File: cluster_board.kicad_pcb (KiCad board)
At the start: 4 copper layers, 200 x 200 mm, 170 parts, among them J1 PICO_UART, J10 TILE_OUT_1, J11 TILE_OUT_2, J12 TILE_OUT_3, J13 TILE_OUT_4, J14 TILE_OUT_5, J15 TILE_OUT_6, J2 BOOT_I2C, J3 TILE_IN, U1 RP2354B, U10 RP2354B, U100 RP2354B, U101 RP2354B, U102 RP2354B, U103 RP2354B, U104 RP2354B, U105 RP2354B, U106 RP2354B, U107 RP2354B, U108 RP2354B, U109 RP2354B, U11 RP2354B, U110 RP2354B, U111 RP2354B, U112 RP2354B, U113 RP2354B, U114 RP2354B, U115 RP2354B, U116 RP2354B, U117 RP2354B, U118 RP2354B, U119 RP2354B, U12 RP2354B, U120 RP2354B, U121 TPS54560_A, U122 TPS54560_B, U13 RP2354B, U130 PCF8574, U131 PCF8574, U132 PCF8574, U133 PCF8574, U134 PCF8574, U135 PCF8574, U136 PCF8574, U137 PCF8574, U138 PCF8574A, U139 PCF8574A, U14 RP2354B, U140 PCF8574A, U141 PCF8574A, U142 PCF8574A, U143 PCF8574A, U144 PCF8574A, U145 74HC244, U146 74HC244, U147 74HC244, U148 74HC244, U149 74HC244, U15 RP2354B, U150 74HC244, U151 74HC244, U152 74HC244, U153 74HC244, U154 74HC244, U155 74HC244, U156 74HC244, U157 74HC244, U158 74HC244, U159 74HC244, U16 RP2354B, U17 RP2354B, U18 RP2354B, U19 RP2354B, U2 RP2354B, U20 RP2354B, U21 RP2354B, U22 RP2354B, U23 RP2354B, U24 RP2354B, U25 RP2354B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

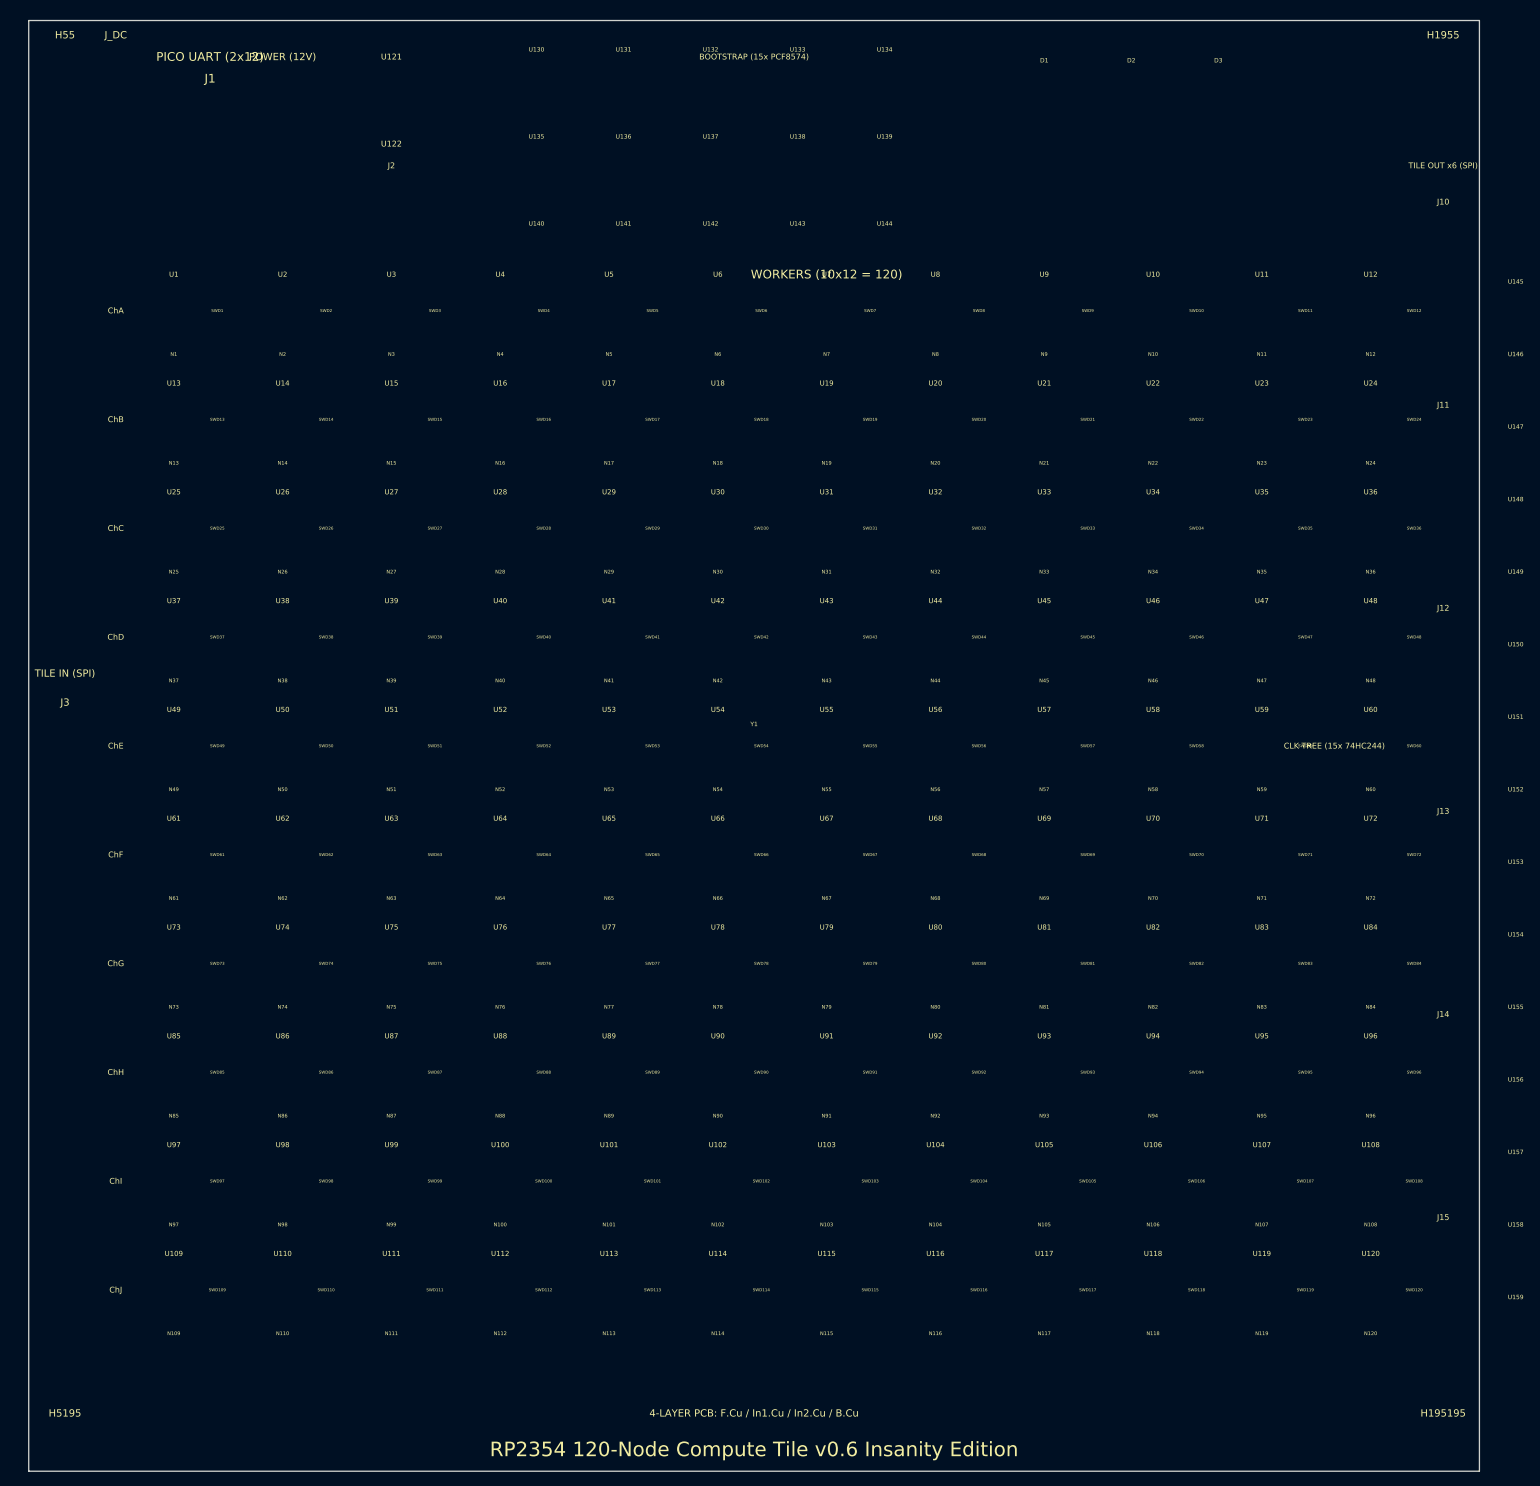
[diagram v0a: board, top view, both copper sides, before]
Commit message: Regenerate KiCad output files for v1.0 architecture
Co-authored-by: Copilot <223556219+Copilot@users.noreply.github.com>
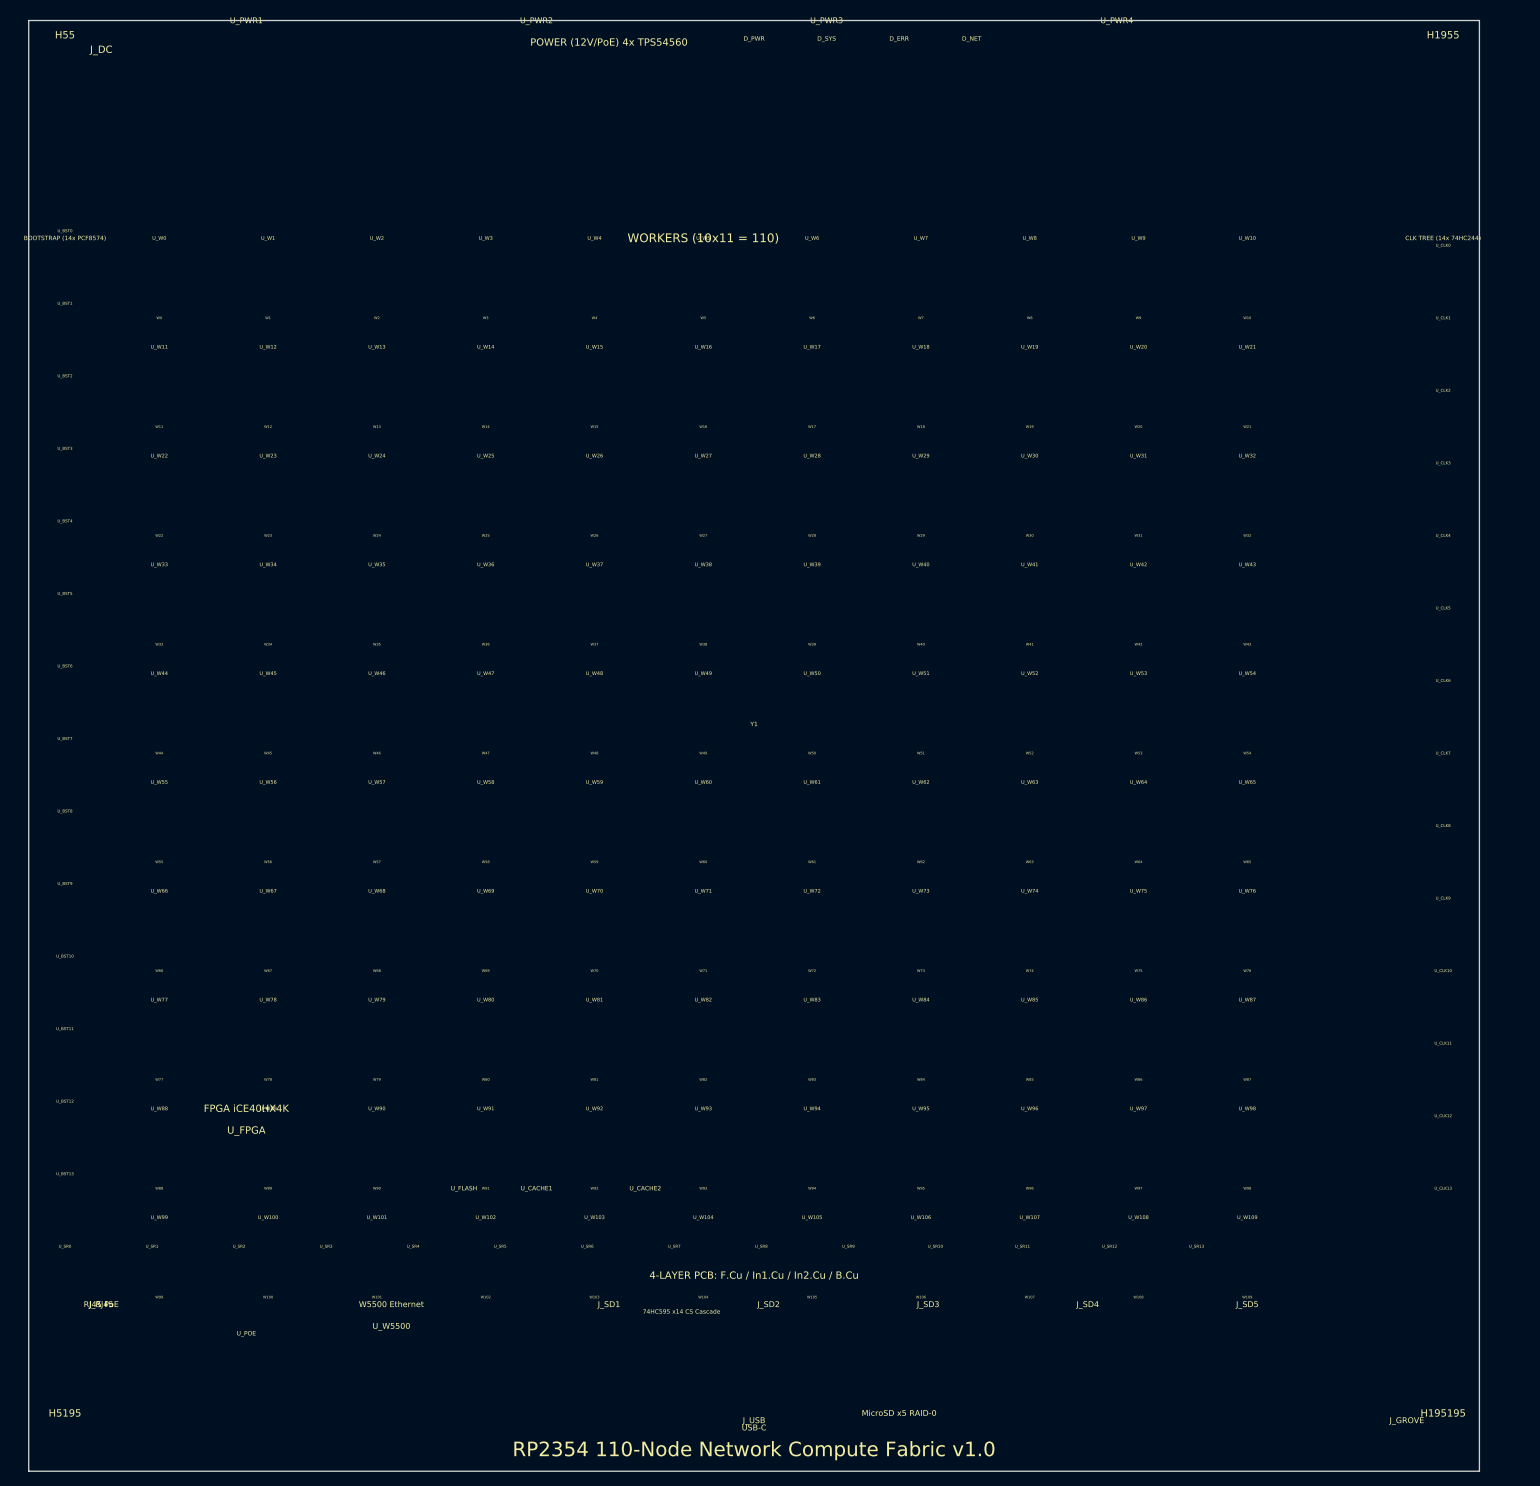
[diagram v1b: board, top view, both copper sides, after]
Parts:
- removed D1: PWR, LED_SMD:LED_0603_1608Metric
- removed D2: SYS, LED_SMD:LED_0603_1608Metric
- removed D3: ERR, LED_SMD:LED_0603_1608Metric
- removed J1: PICO_UART, Connector_PinHeader_2.54mm:PinHeader_2x12_P2.54mm_Vertical
- removed J10: TILE_OUT_1, Connector_JST:JST_PH_B4B-PH-K_1x04_P2.00mm_Vertical
- removed J11: TILE_OUT_2, Connector_JST:JST_PH_B4B-PH-K_1x04_P2.00mm_Vertical
- removed J12: TILE_OUT_3, Connector_JST:JST_PH_B4B-PH-K_1x04_P2.00mm_Vertical
- removed J13: TILE_OUT_4, Connector_JST:JST_PH_B4B-PH-K_1x04_P2.00mm_Vertical
- removed J14: TILE_OUT_5, Connector_JST:JST_PH_B4B-PH-K_1x04_P2.00mm_Vertical
- removed J15: TILE_OUT_6, Connector_JST:JST_PH_B4B-PH-K_1x04_P2.00mm_Vertical
- removed J2: BOOT_I2C, Connector_JST:JST_PH_B4B-PH-K_1x04_P2.00mm_Vertical
- removed J3: TILE_IN, Connector_JST:JST_PH_B4B-PH-K_1x04_P2.00mm_Vertical
- removed the J_DC at (12.0, 8.00)
- removed U1, U10, U100, U101, U102, U103, U104, U105, U106, U107, U108, U109, U11, U110, U111, U112, U113, U114, U115, U116, U117, U118, U119, U12, U120, U13, U14, U15, U16, U17, U18, U19, U2, U20, U21, U22, U23, U24, U25, U26, U27, U28, U29, U3, U30, U31, U32, U33, U34, U35, U36, U37, U38, U39, U4, U40, U41, U42, U43, U44, U45, U46, U47, U48, U49, U5, U50, U51, U52, U53, U54, U55, U56, U57, U58, U59, U6, U60, U61, U62, U63, U64, U65, U66, U67, U68, U69, U7, U70, U71, U72, U73, U74, U75, U76, U77, U78, U79, U8, U80, U81, U82, U83, U84, U85, U86, U87, U88, U89, U9, U90, U91, U92, U93, U94, U95, U96, U97, U98, U99: RP2354B, Package_DFN_QFN:QFN-80-1EP_10x10mm_P0.4mm_EP5.45x5.45mm
- removed U121: TPS54560_A, Package_SO:HSOP-8-1EP_3.9x4.9mm_P1.27mm_EP2.41x3.1mm
- removed U122: TPS54560_B, Package_SO:HSOP-8-1EP_3.9x4.9mm_P1.27mm_EP2.41x3.1mm
- removed U130, U131, U132, U133, U134, U135, U136, U137: PCF8574, Package_SO:SOIC-16_3.9x9.9mm_P1.27mm
- removed U138, U139, U140, U141, U142, U143, U144: PCF8574A, Package_SO:SOIC-16_3.9x9.9mm_P1.27mm
- removed U145, U146, U147, U148, U149, U150, U151, U152, U153, U154, U155, U156, U157, U158, U159: 74HC244, Package_SO:TSSOP-20_4.4x6.5mm_P0.65mm
- added D_ERR: ERR, LED_SMD:LED_0603_1608Metric, F.Cu at (120.0, 5.00)
- added D_NET: NET, LED_SMD:LED_0603_1608Metric, F.Cu at (130.0, 5.00)
- added D_PWR: PWR, LED_SMD:LED_0603_1608Metric, F.Cu at (100.0, 5.00)
- added D_SYS: SYS, LED_SMD:LED_0603_1608Metric, F.Cu at (110.0, 5.00)
- added J_DC: 12V_DC, TerminalBlock_Phoenix:TerminalBlock_Phoenix_PT-1,5-2-5.0-H_1x02_P5.00mm_Horizontal, F.Cu at (10.0, 10.0)
- added J_GROVE: Grove_I2C, Connector_JST:JST_PH_B4B-PH-K_1x04_P2.00mm_Vertical, F.Cu at (190.0, 198.0)
- added J_RJ45: RJ45_PoE, Connector_RJ:RJ45_Amphenol_ARJM11D7-805-AB-EW2, F.Cu at (10.0, 185.0)
- added J_SD1: MicroSD_1, Connector_Card:microSD_HC_Molex_104031-0811, F.Cu at (80.0, 185.0)
- added J_SD2: MicroSD_2, Connector_Card:microSD_HC_Molex_104031-0811, F.Cu at (102.0, 185.0)
- added J_SD3: MicroSD_3, Connector_Card:microSD_HC_Molex_104031-0811, F.Cu at (124.0, 185.0)
- added J_SD4: MicroSD_4, Connector_Card:microSD_HC_Molex_104031-0811, F.Cu at (146.0, 185.0)
- added J_SD5: MicroSD_5, Connector_Card:microSD_HC_Molex_104031-0811, F.Cu at (168.0, 185.0)
- added J_USB: USB_C, Connector_USB:USB_C_Receptacle_GCT_USB4105-xx-A_16P_TopMount_Horizontal, F.Cu at (100.0, 198.0)
- added U_BST0: PCF8574, Package_SO:SOIC-16_3.9x9.9mm_P1.27mm, F.Cu at (5.00, 35.0)
- added U_BST1: PCF8574, Package_SO:SOIC-16_3.9x9.9mm_P1.27mm, F.Cu at (5.00, 45.0)
- added U_BST10: PCF8574, Package_SO:SOIC-16_3.9x9.9mm_P1.27mm, F.Cu at (5.00, 135.0)
- added U_BST11: PCF8574, Package_SO:SOIC-16_3.9x9.9mm_P1.27mm, F.Cu at (5.00, 145.0)
- added U_BST12: PCF8574, Package_SO:SOIC-16_3.9x9.9mm_P1.27mm, F.Cu at (5.00, 155.0)
- added U_BST13: PCF8574, Package_SO:SOIC-16_3.9x9.9mm_P1.27mm, F.Cu at (5.00, 165.0)
- added U_BST2: PCF8574, Package_SO:SOIC-16_3.9x9.9mm_P1.27mm, F.Cu at (5.00, 55.0)
- added U_BST3: PCF8574, Package_SO:SOIC-16_3.9x9.9mm_P1.27mm, F.Cu at (5.00, 65.0)
- added U_BST4: PCF8574, Package_SO:SOIC-16_3.9x9.9mm_P1.27mm, F.Cu at (5.00, 75.0)
- added U_BST5: PCF8574, Package_SO:SOIC-16_3.9x9.9mm_P1.27mm, F.Cu at (5.00, 85.0)
- added U_BST6: PCF8574, Package_SO:SOIC-16_3.9x9.9mm_P1.27mm, F.Cu at (5.00, 95.0)
- added U_BST7: PCF8574, Package_SO:SOIC-16_3.9x9.9mm_P1.27mm, F.Cu at (5.00, 105.0)
- added U_BST8: PCF8574, Package_SO:SOIC-16_3.9x9.9mm_P1.27mm, F.Cu at (5.00, 115.0)
- added U_BST9: PCF8574, Package_SO:SOIC-16_3.9x9.9mm_P1.27mm, F.Cu at (5.00, 125.0)
- added U_CACHE1: APS6404L, Package_SO:SOP-8_3.9x4.9mm_P1.27mm, F.Cu at (70.0, 165.0)
- added U_CACHE2: APS6404L, Package_SO:SOP-8_3.9x4.9mm_P1.27mm, F.Cu at (85.0, 165.0)
- added U_CLK0: 74HC244, Package_SO:TSSOP-20_4.4x6.5mm_P0.65mm, F.Cu at (195.0, 35.0)
- added U_CLK1: 74HC244, Package_SO:TSSOP-20_4.4x6.5mm_P0.65mm, F.Cu at (195.0, 45.0)
- added U_CLK10: 74HC244, Package_SO:TSSOP-20_4.4x6.5mm_P0.65mm, F.Cu at (195.0, 135.0)
- added U_CLK11: 74HC244, Package_SO:TSSOP-20_4.4x6.5mm_P0.65mm, F.Cu at (195.0, 145.0)
- added U_CLK12: 74HC244, Package_SO:TSSOP-20_4.4x6.5mm_P0.65mm, F.Cu at (195.0, 155.0)
- added U_CLK13: 74HC244, Package_SO:TSSOP-20_4.4x6.5mm_P0.65mm, F.Cu at (195.0, 165.0)
- added U_CLK2: 74HC244, Package_SO:TSSOP-20_4.4x6.5mm_P0.65mm, F.Cu at (195.0, 55.0)
- added U_CLK3: 74HC244, Package_SO:TSSOP-20_4.4x6.5mm_P0.65mm, F.Cu at (195.0, 65.0)
- added U_CLK4: 74HC244, Package_SO:TSSOP-20_4.4x6.5mm_P0.65mm, F.Cu at (195.0, 75.0)
- added U_CLK5: 74HC244, Package_SO:TSSOP-20_4.4x6.5mm_P0.65mm, F.Cu at (195.0, 85.0)
- added U_CLK6: 74HC244, Package_SO:TSSOP-20_4.4x6.5mm_P0.65mm, F.Cu at (195.0, 95.0)
- added U_CLK7: 74HC244, Package_SO:TSSOP-20_4.4x6.5mm_P0.65mm, F.Cu at (195.0, 105.0)
- added U_CLK8: 74HC244, Package_SO:TSSOP-20_4.4x6.5mm_P0.65mm, F.Cu at (195.0, 115.0)
- added U_CLK9: 74HC244, Package_SO:TSSOP-20_4.4x6.5mm_P0.65mm, F.Cu at (195.0, 125.0)
- added U_FLASH: W25Q32, Package_SO:SOIC-8_3.9x4.9mm_P1.27mm, F.Cu at (60.0, 165.0)
- added U_FPGA: iCE40HX4K, Package_QFP:TQFP-144_20x20mm_P0.5mm, F.Cu at (30.0, 165.0)
- added U_POE: Ag9905, Package_SO:SOP-8_3.9x4.9mm_P1.27mm, F.Cu at (30.0, 185.0)
- added U_PSRAM0: LY68L6400, Package_SO:SOP-8_3.9x4.9mm_P1.27mm, B.Cu at (18.0, 35.0)
- added U_PSRAM1: LY68L6400, Package_SO:SOP-8_3.9x4.9mm_P1.27mm, B.Cu at (33.0, 35.0)
- added U_PSRAM10: LY68L6400, Package_SO:SOP-8_3.9x4.9mm_P1.27mm, B.Cu at (168.0, 35.0)
- added U_PSRAM100: LY68L6400, Package_SO:SOP-8_3.9x4.9mm_P1.27mm, B.Cu at (33.0, 170.0)
- added U_PSRAM101: LY68L6400, Package_SO:SOP-8_3.9x4.9mm_P1.27mm, B.Cu at (48.0, 170.0)
- added U_PSRAM102: LY68L6400, Package_SO:SOP-8_3.9x4.9mm_P1.27mm, B.Cu at (63.0, 170.0)
- added U_PSRAM103: LY68L6400, Package_SO:SOP-8_3.9x4.9mm_P1.27mm, B.Cu at (78.0, 170.0)
- added U_PSRAM104: LY68L6400, Package_SO:SOP-8_3.9x4.9mm_P1.27mm, B.Cu at (93.0, 170.0)
- added U_PSRAM105: LY68L6400, Package_SO:SOP-8_3.9x4.9mm_P1.27mm, B.Cu at (108.0, 170.0)
- added U_PSRAM106: LY68L6400, Package_SO:SOP-8_3.9x4.9mm_P1.27mm, B.Cu at (123.0, 170.0)
- added U_PSRAM107: LY68L6400, Package_SO:SOP-8_3.9x4.9mm_P1.27mm, B.Cu at (138.0, 170.0)
- added U_PSRAM108: LY68L6400, Package_SO:SOP-8_3.9x4.9mm_P1.27mm, B.Cu at (153.0, 170.0)
- added U_PSRAM109: LY68L6400, Package_SO:SOP-8_3.9x4.9mm_P1.27mm, B.Cu at (168.0, 170.0)
- added U_PSRAM11: LY68L6400, Package_SO:SOP-8_3.9x4.9mm_P1.27mm, B.Cu at (18.0, 50.0)
- added U_PSRAM12: LY68L6400, Package_SO:SOP-8_3.9x4.9mm_P1.27mm, B.Cu at (33.0, 50.0)
- added U_PSRAM13: LY68L6400, Package_SO:SOP-8_3.9x4.9mm_P1.27mm, B.Cu at (48.0, 50.0)
- added U_PSRAM14: LY68L6400, Package_SO:SOP-8_3.9x4.9mm_P1.27mm, B.Cu at (63.0, 50.0)
- added U_PSRAM15: LY68L6400, Package_SO:SOP-8_3.9x4.9mm_P1.27mm, B.Cu at (78.0, 50.0)
- added U_PSRAM16: LY68L6400, Package_SO:SOP-8_3.9x4.9mm_P1.27mm, B.Cu at (93.0, 50.0)
- added U_PSRAM17: LY68L6400, Package_SO:SOP-8_3.9x4.9mm_P1.27mm, B.Cu at (108.0, 50.0)
- added U_PSRAM18: LY68L6400, Package_SO:SOP-8_3.9x4.9mm_P1.27mm, B.Cu at (123.0, 50.0)
- added U_PSRAM19: LY68L6400, Package_SO:SOP-8_3.9x4.9mm_P1.27mm, B.Cu at (138.0, 50.0)
- added U_PSRAM2: LY68L6400, Package_SO:SOP-8_3.9x4.9mm_P1.27mm, B.Cu at (48.0, 35.0)
- added U_PSRAM20: LY68L6400, Package_SO:SOP-8_3.9x4.9mm_P1.27mm, B.Cu at (153.0, 50.0)
- added U_PSRAM21: LY68L6400, Package_SO:SOP-8_3.9x4.9mm_P1.27mm, B.Cu at (168.0, 50.0)
- added U_PSRAM22: LY68L6400, Package_SO:SOP-8_3.9x4.9mm_P1.27mm, B.Cu at (18.0, 65.0)
- added U_PSRAM23: LY68L6400, Package_SO:SOP-8_3.9x4.9mm_P1.27mm, B.Cu at (33.0, 65.0)
- added U_PSRAM24: LY68L6400, Package_SO:SOP-8_3.9x4.9mm_P1.27mm, B.Cu at (48.0, 65.0)
- added U_PSRAM25: LY68L6400, Package_SO:SOP-8_3.9x4.9mm_P1.27mm, B.Cu at (63.0, 65.0)
- added U_PSRAM26: LY68L6400, Package_SO:SOP-8_3.9x4.9mm_P1.27mm, B.Cu at (78.0, 65.0)
- added U_PSRAM27: LY68L6400, Package_SO:SOP-8_3.9x4.9mm_P1.27mm, B.Cu at (93.0, 65.0)
- added U_PSRAM28: LY68L6400, Package_SO:SOP-8_3.9x4.9mm_P1.27mm, B.Cu at (108.0, 65.0)
- added U_PSRAM29: LY68L6400, Package_SO:SOP-8_3.9x4.9mm_P1.27mm, B.Cu at (123.0, 65.0)
- added U_PSRAM3: LY68L6400, Package_SO:SOP-8_3.9x4.9mm_P1.27mm, B.Cu at (63.0, 35.0)
- added U_PSRAM30: LY68L6400, Package_SO:SOP-8_3.9x4.9mm_P1.27mm, B.Cu at (138.0, 65.0)
- added U_PSRAM31: LY68L6400, Package_SO:SOP-8_3.9x4.9mm_P1.27mm, B.Cu at (153.0, 65.0)
- added U_PSRAM32: LY68L6400, Package_SO:SOP-8_3.9x4.9mm_P1.27mm, B.Cu at (168.0, 65.0)
- added U_PSRAM33: LY68L6400, Package_SO:SOP-8_3.9x4.9mm_P1.27mm, B.Cu at (18.0, 80.0)
- added U_PSRAM34: LY68L6400, Package_SO:SOP-8_3.9x4.9mm_P1.27mm, B.Cu at (33.0, 80.0)
- added U_PSRAM35: LY68L6400, Package_SO:SOP-8_3.9x4.9mm_P1.27mm, B.Cu at (48.0, 80.0)
- added U_PSRAM36: LY68L6400, Package_SO:SOP-8_3.9x4.9mm_P1.27mm, B.Cu at (63.0, 80.0)
- added U_PSRAM37: LY68L6400, Package_SO:SOP-8_3.9x4.9mm_P1.27mm, B.Cu at (78.0, 80.0)
- added U_PSRAM38: LY68L6400, Package_SO:SOP-8_3.9x4.9mm_P1.27mm, B.Cu at (93.0, 80.0)
- added U_PSRAM39: LY68L6400, Package_SO:SOP-8_3.9x4.9mm_P1.27mm, B.Cu at (108.0, 80.0)
- added U_PSRAM4: LY68L6400, Package_SO:SOP-8_3.9x4.9mm_P1.27mm, B.Cu at (78.0, 35.0)
- added U_PSRAM40: LY68L6400, Package_SO:SOP-8_3.9x4.9mm_P1.27mm, B.Cu at (123.0, 80.0)
- added U_PSRAM41: LY68L6400, Package_SO:SOP-8_3.9x4.9mm_P1.27mm, B.Cu at (138.0, 80.0)
- added U_PSRAM42: LY68L6400, Package_SO:SOP-8_3.9x4.9mm_P1.27mm, B.Cu at (153.0, 80.0)
- added U_PSRAM43: LY68L6400, Package_SO:SOP-8_3.9x4.9mm_P1.27mm, B.Cu at (168.0, 80.0)
- added U_PSRAM44: LY68L6400, Package_SO:SOP-8_3.9x4.9mm_P1.27mm, B.Cu at (18.0, 95.0)
- added U_PSRAM45: LY68L6400, Package_SO:SOP-8_3.9x4.9mm_P1.27mm, B.Cu at (33.0, 95.0)
- added U_PSRAM46: LY68L6400, Package_SO:SOP-8_3.9x4.9mm_P1.27mm, B.Cu at (48.0, 95.0)
- added U_PSRAM47: LY68L6400, Package_SO:SOP-8_3.9x4.9mm_P1.27mm, B.Cu at (63.0, 95.0)
- added U_PSRAM48: LY68L6400, Package_SO:SOP-8_3.9x4.9mm_P1.27mm, B.Cu at (78.0, 95.0)
- added U_PSRAM49: LY68L6400, Package_SO:SOP-8_3.9x4.9mm_P1.27mm, B.Cu at (93.0, 95.0)
- added U_PSRAM5: LY68L6400, Package_SO:SOP-8_3.9x4.9mm_P1.27mm, B.Cu at (93.0, 35.0)
- added U_PSRAM50: LY68L6400, Package_SO:SOP-8_3.9x4.9mm_P1.27mm, B.Cu at (108.0, 95.0)
- added U_PSRAM51: LY68L6400, Package_SO:SOP-8_3.9x4.9mm_P1.27mm, B.Cu at (123.0, 95.0)
- added U_PSRAM52: LY68L6400, Package_SO:SOP-8_3.9x4.9mm_P1.27mm, B.Cu at (138.0, 95.0)
- added U_PSRAM53: LY68L6400, Package_SO:SOP-8_3.9x4.9mm_P1.27mm, B.Cu at (153.0, 95.0)
- added U_PSRAM54: LY68L6400, Package_SO:SOP-8_3.9x4.9mm_P1.27mm, B.Cu at (168.0, 95.0)
- added U_PSRAM55: LY68L6400, Package_SO:SOP-8_3.9x4.9mm_P1.27mm, B.Cu at (18.0, 110.0)
- added U_PSRAM56: LY68L6400, Package_SO:SOP-8_3.9x4.9mm_P1.27mm, B.Cu at (33.0, 110.0)
- added U_PSRAM57: LY68L6400, Package_SO:SOP-8_3.9x4.9mm_P1.27mm, B.Cu at (48.0, 110.0)
- added U_PSRAM58: LY68L6400, Package_SO:SOP-8_3.9x4.9mm_P1.27mm, B.Cu at (63.0, 110.0)
- added U_PSRAM59: LY68L6400, Package_SO:SOP-8_3.9x4.9mm_P1.27mm, B.Cu at (78.0, 110.0)
- added U_PSRAM6: LY68L6400, Package_SO:SOP-8_3.9x4.9mm_P1.27mm, B.Cu at (108.0, 35.0)
- added U_PSRAM60: LY68L6400, Package_SO:SOP-8_3.9x4.9mm_P1.27mm, B.Cu at (93.0, 110.0)
- added U_PSRAM61: LY68L6400, Package_SO:SOP-8_3.9x4.9mm_P1.27mm, B.Cu at (108.0, 110.0)
- added U_PSRAM62: LY68L6400, Package_SO:SOP-8_3.9x4.9mm_P1.27mm, B.Cu at (123.0, 110.0)
- added U_PSRAM63: LY68L6400, Package_SO:SOP-8_3.9x4.9mm_P1.27mm, B.Cu at (138.0, 110.0)
- added U_PSRAM64: LY68L6400, Package_SO:SOP-8_3.9x4.9mm_P1.27mm, B.Cu at (153.0, 110.0)
- added U_PSRAM65: LY68L6400, Package_SO:SOP-8_3.9x4.9mm_P1.27mm, B.Cu at (168.0, 110.0)
- added U_PSRAM66: LY68L6400, Package_SO:SOP-8_3.9x4.9mm_P1.27mm, B.Cu at (18.0, 125.0)
- added U_PSRAM67: LY68L6400, Package_SO:SOP-8_3.9x4.9mm_P1.27mm, B.Cu at (33.0, 125.0)
- added U_PSRAM68: LY68L6400, Package_SO:SOP-8_3.9x4.9mm_P1.27mm, B.Cu at (48.0, 125.0)
- added U_PSRAM69: LY68L6400, Package_SO:SOP-8_3.9x4.9mm_P1.27mm, B.Cu at (63.0, 125.0)
- added U_PSRAM7: LY68L6400, Package_SO:SOP-8_3.9x4.9mm_P1.27mm, B.Cu at (123.0, 35.0)
- added U_PSRAM70: LY68L6400, Package_SO:SOP-8_3.9x4.9mm_P1.27mm, B.Cu at (78.0, 125.0)
- added U_PSRAM71: LY68L6400, Package_SO:SOP-8_3.9x4.9mm_P1.27mm, B.Cu at (93.0, 125.0)
- added U_PSRAM72: LY68L6400, Package_SO:SOP-8_3.9x4.9mm_P1.27mm, B.Cu at (108.0, 125.0)
- added U_PSRAM73: LY68L6400, Package_SO:SOP-8_3.9x4.9mm_P1.27mm, B.Cu at (123.0, 125.0)
- added U_PSRAM74: LY68L6400, Package_SO:SOP-8_3.9x4.9mm_P1.27mm, B.Cu at (138.0, 125.0)
- added U_PSRAM75: LY68L6400, Package_SO:SOP-8_3.9x4.9mm_P1.27mm, B.Cu at (153.0, 125.0)
- added U_PSRAM76: LY68L6400, Package_SO:SOP-8_3.9x4.9mm_P1.27mm, B.Cu at (168.0, 125.0)
- added U_PSRAM77: LY68L6400, Package_SO:SOP-8_3.9x4.9mm_P1.27mm, B.Cu at (18.0, 140.0)
- added U_PSRAM78: LY68L6400, Package_SO:SOP-8_3.9x4.9mm_P1.27mm, B.Cu at (33.0, 140.0)
- added U_PSRAM79: LY68L6400, Package_SO:SOP-8_3.9x4.9mm_P1.27mm, B.Cu at (48.0, 140.0)
- added U_PSRAM8: LY68L6400, Package_SO:SOP-8_3.9x4.9mm_P1.27mm, B.Cu at (138.0, 35.0)
- added U_PSRAM80: LY68L6400, Package_SO:SOP-8_3.9x4.9mm_P1.27mm, B.Cu at (63.0, 140.0)
- added U_PSRAM81: LY68L6400, Package_SO:SOP-8_3.9x4.9mm_P1.27mm, B.Cu at (78.0, 140.0)
- added U_PSRAM82: LY68L6400, Package_SO:SOP-8_3.9x4.9mm_P1.27mm, B.Cu at (93.0, 140.0)
- added U_PSRAM83: LY68L6400, Package_SO:SOP-8_3.9x4.9mm_P1.27mm, B.Cu at (108.0, 140.0)
- added U_PSRAM84: LY68L6400, Package_SO:SOP-8_3.9x4.9mm_P1.27mm, B.Cu at (123.0, 140.0)
- added U_PSRAM85: LY68L6400, Package_SO:SOP-8_3.9x4.9mm_P1.27mm, B.Cu at (138.0, 140.0)
- added U_PSRAM86: LY68L6400, Package_SO:SOP-8_3.9x4.9mm_P1.27mm, B.Cu at (153.0, 140.0)
- added U_PSRAM87: LY68L6400, Package_SO:SOP-8_3.9x4.9mm_P1.27mm, B.Cu at (168.0, 140.0)
- added U_PSRAM88: LY68L6400, Package_SO:SOP-8_3.9x4.9mm_P1.27mm, B.Cu at (18.0, 155.0)
- added U_PSRAM89: LY68L6400, Package_SO:SOP-8_3.9x4.9mm_P1.27mm, B.Cu at (33.0, 155.0)
- added U_PSRAM9: LY68L6400, Package_SO:SOP-8_3.9x4.9mm_P1.27mm, B.Cu at (153.0, 35.0)
- added U_PSRAM90: LY68L6400, Package_SO:SOP-8_3.9x4.9mm_P1.27mm, B.Cu at (48.0, 155.0)
- added U_PSRAM91: LY68L6400, Package_SO:SOP-8_3.9x4.9mm_P1.27mm, B.Cu at (63.0, 155.0)
- added U_PSRAM92: LY68L6400, Package_SO:SOP-8_3.9x4.9mm_P1.27mm, B.Cu at (78.0, 155.0)
- added U_PSRAM93: LY68L6400, Package_SO:SOP-8_3.9x4.9mm_P1.27mm, B.Cu at (93.0, 155.0)
- added U_PSRAM94: LY68L6400, Package_SO:SOP-8_3.9x4.9mm_P1.27mm, B.Cu at (108.0, 155.0)
- added U_PSRAM95: LY68L6400, Package_SO:SOP-8_3.9x4.9mm_P1.27mm, B.Cu at (123.0, 155.0)
- added U_PSRAM96: LY68L6400, Package_SO:SOP-8_3.9x4.9mm_P1.27mm, B.Cu at (138.0, 155.0)
- added U_PSRAM97: LY68L6400, Package_SO:SOP-8_3.9x4.9mm_P1.27mm, B.Cu at (153.0, 155.0)
- added U_PSRAM98: LY68L6400, Package_SO:SOP-8_3.9x4.9mm_P1.27mm, B.Cu at (168.0, 155.0)
- added U_PSRAM99: LY68L6400, Package_SO:SOP-8_3.9x4.9mm_P1.27mm, B.Cu at (18.0, 170.0)
- added U_PWR1: TPS54560_Z1, Package_SO:HSOP-8-1EP_3.9x4.9mm_P1.27mm_EP2.41x3.1mm, F.Cu at (30.0, 5.00)
- added U_PWR2: TPS54560_Z2, Package_SO:HSOP-8-1EP_3.9x4.9mm_P1.27mm_EP2.41x3.1mm, F.Cu at (70.0, 5.00)
- added U_PWR3: TPS54560_Z3, Package_SO:HSOP-8-1EP_3.9x4.9mm_P1.27mm_EP2.41x3.1mm, F.Cu at (110.0, 5.00)
- added U_PWR4: TPS54560_Z4, Package_SO:HSOP-8-1EP_3.9x4.9mm_P1.27mm_EP2.41x3.1mm, F.Cu at (150.0, 5.00)
- added U_SR0: 74HC595, Package_SO:SOIC-16_3.9x9.9mm_P1.27mm, F.Cu at (5.00, 175.0)
- added U_SR1: 74HC595, Package_SO:SOIC-16_3.9x9.9mm_P1.27mm, F.Cu at (17.0, 175.0)
- added U_SR10: 74HC595, Package_SO:SOIC-16_3.9x9.9mm_P1.27mm, F.Cu at (125.0, 175.0)
- added U_SR11: 74HC595, Package_SO:SOIC-16_3.9x9.9mm_P1.27mm, F.Cu at (137.0, 175.0)
- added U_SR12: 74HC595, Package_SO:SOIC-16_3.9x9.9mm_P1.27mm, F.Cu at (149.0, 175.0)
- added U_SR13: 74HC595, Package_SO:SOIC-16_3.9x9.9mm_P1.27mm, F.Cu at (161.0, 175.0)
- added U_SR2: 74HC595, Package_SO:SOIC-16_3.9x9.9mm_P1.27mm, F.Cu at (29.0, 175.0)
- added U_SR3: 74HC595, Package_SO:SOIC-16_3.9x9.9mm_P1.27mm, F.Cu at (41.0, 175.0)
- added U_SR4: 74HC595, Package_SO:SOIC-16_3.9x9.9mm_P1.27mm, F.Cu at (53.0, 175.0)
- added U_SR5: 74HC595, Package_SO:SOIC-16_3.9x9.9mm_P1.27mm, F.Cu at (65.0, 175.0)
- added U_SR6: 74HC595, Package_SO:SOIC-16_3.9x9.9mm_P1.27mm, F.Cu at (77.0, 175.0)
- added U_SR7: 74HC595, Package_SO:SOIC-16_3.9x9.9mm_P1.27mm, F.Cu at (89.0, 175.0)
- added U_SR8: 74HC595, Package_SO:SOIC-16_3.9x9.9mm_P1.27mm, F.Cu at (101.0, 175.0)
- added U_SR9: 74HC595, Package_SO:SOIC-16_3.9x9.9mm_P1.27mm, F.Cu at (113.0, 175.0)
- added U_W0: RP2354B, Package_DFN_QFN:QFN-80-1EP_10x10mm_P0.4mm_EP5.45x5.45mm, F.Cu at (18.0, 35.0)
- added U_W1: RP2354B, Package_DFN_QFN:QFN-80-1EP_10x10mm_P0.4mm_EP5.45x5.45mm, F.Cu at (33.0, 35.0)
- added U_W10: RP2354B, Package_DFN_QFN:QFN-80-1EP_10x10mm_P0.4mm_EP5.45x5.45mm, F.Cu at (168.0, 35.0)
- added U_W100: RP2354B, Package_DFN_QFN:QFN-80-1EP_10x10mm_P0.4mm_EP5.45x5.45mm, F.Cu at (33.0, 170.0)
- added U_W101: RP2354B, Package_DFN_QFN:QFN-80-1EP_10x10mm_P0.4mm_EP5.45x5.45mm, F.Cu at (48.0, 170.0)
- added U_W102: RP2354B, Package_DFN_QFN:QFN-80-1EP_10x10mm_P0.4mm_EP5.45x5.45mm, F.Cu at (63.0, 170.0)
- added U_W103: RP2354B, Package_DFN_QFN:QFN-80-1EP_10x10mm_P0.4mm_EP5.45x5.45mm, F.Cu at (78.0, 170.0)
- added U_W104: RP2354B, Package_DFN_QFN:QFN-80-1EP_10x10mm_P0.4mm_EP5.45x5.45mm, F.Cu at (93.0, 170.0)
- added U_W105: RP2354B, Package_DFN_QFN:QFN-80-1EP_10x10mm_P0.4mm_EP5.45x5.45mm, F.Cu at (108.0, 170.0)
- added U_W106: RP2354B, Package_DFN_QFN:QFN-80-1EP_10x10mm_P0.4mm_EP5.45x5.45mm, F.Cu at (123.0, 170.0)
- added U_W107: RP2354B, Package_DFN_QFN:QFN-80-1EP_10x10mm_P0.4mm_EP5.45x5.45mm, F.Cu at (138.0, 170.0)
- added U_W108: RP2354B, Package_DFN_QFN:QFN-80-1EP_10x10mm_P0.4mm_EP5.45x5.45mm, F.Cu at (153.0, 170.0)
- added U_W109: RP2354B, Package_DFN_QFN:QFN-80-1EP_10x10mm_P0.4mm_EP5.45x5.45mm, F.Cu at (168.0, 170.0)
- added U_W11: RP2354B, Package_DFN_QFN:QFN-80-1EP_10x10mm_P0.4mm_EP5.45x5.45mm, F.Cu at (18.0, 50.0)
- added U_W12: RP2354B, Package_DFN_QFN:QFN-80-1EP_10x10mm_P0.4mm_EP5.45x5.45mm, F.Cu at (33.0, 50.0)
- added U_W13: RP2354B, Package_DFN_QFN:QFN-80-1EP_10x10mm_P0.4mm_EP5.45x5.45mm, F.Cu at (48.0, 50.0)
- added U_W14: RP2354B, Package_DFN_QFN:QFN-80-1EP_10x10mm_P0.4mm_EP5.45x5.45mm, F.Cu at (63.0, 50.0)
- added U_W15: RP2354B, Package_DFN_QFN:QFN-80-1EP_10x10mm_P0.4mm_EP5.45x5.45mm, F.Cu at (78.0, 50.0)
- added U_W16: RP2354B, Package_DFN_QFN:QFN-80-1EP_10x10mm_P0.4mm_EP5.45x5.45mm, F.Cu at (93.0, 50.0)
- added U_W17: RP2354B, Package_DFN_QFN:QFN-80-1EP_10x10mm_P0.4mm_EP5.45x5.45mm, F.Cu at (108.0, 50.0)
- added U_W18: RP2354B, Package_DFN_QFN:QFN-80-1EP_10x10mm_P0.4mm_EP5.45x5.45mm, F.Cu at (123.0, 50.0)
- added U_W19: RP2354B, Package_DFN_QFN:QFN-80-1EP_10x10mm_P0.4mm_EP5.45x5.45mm, F.Cu at (138.0, 50.0)
- added U_W2: RP2354B, Package_DFN_QFN:QFN-80-1EP_10x10mm_P0.4mm_EP5.45x5.45mm, F.Cu at (48.0, 35.0)
- added U_W20: RP2354B, Package_DFN_QFN:QFN-80-1EP_10x10mm_P0.4mm_EP5.45x5.45mm, F.Cu at (153.0, 50.0)
- added U_W21: RP2354B, Package_DFN_QFN:QFN-80-1EP_10x10mm_P0.4mm_EP5.45x5.45mm, F.Cu at (168.0, 50.0)
- added U_W22: RP2354B, Package_DFN_QFN:QFN-80-1EP_10x10mm_P0.4mm_EP5.45x5.45mm, F.Cu at (18.0, 65.0)
- added U_W23: RP2354B, Package_DFN_QFN:QFN-80-1EP_10x10mm_P0.4mm_EP5.45x5.45mm, F.Cu at (33.0, 65.0)
- added U_W24: RP2354B, Package_DFN_QFN:QFN-80-1EP_10x10mm_P0.4mm_EP5.45x5.45mm, F.Cu at (48.0, 65.0)
- added U_W25: RP2354B, Package_DFN_QFN:QFN-80-1EP_10x10mm_P0.4mm_EP5.45x5.45mm, F.Cu at (63.0, 65.0)
- added U_W26: RP2354B, Package_DFN_QFN:QFN-80-1EP_10x10mm_P0.4mm_EP5.45x5.45mm, F.Cu at (78.0, 65.0)
- added U_W27: RP2354B, Package_DFN_QFN:QFN-80-1EP_10x10mm_P0.4mm_EP5.45x5.45mm, F.Cu at (93.0, 65.0)
- added U_W28: RP2354B, Package_DFN_QFN:QFN-80-1EP_10x10mm_P0.4mm_EP5.45x5.45mm, F.Cu at (108.0, 65.0)
- added U_W29: RP2354B, Package_DFN_QFN:QFN-80-1EP_10x10mm_P0.4mm_EP5.45x5.45mm, F.Cu at (123.0, 65.0)
- added U_W3: RP2354B, Package_DFN_QFN:QFN-80-1EP_10x10mm_P0.4mm_EP5.45x5.45mm, F.Cu at (63.0, 35.0)
- added U_W30: RP2354B, Package_DFN_QFN:QFN-80-1EP_10x10mm_P0.4mm_EP5.45x5.45mm, F.Cu at (138.0, 65.0)
- added U_W31: RP2354B, Package_DFN_QFN:QFN-80-1EP_10x10mm_P0.4mm_EP5.45x5.45mm, F.Cu at (153.0, 65.0)
- added U_W32: RP2354B, Package_DFN_QFN:QFN-80-1EP_10x10mm_P0.4mm_EP5.45x5.45mm, F.Cu at (168.0, 65.0)
- added U_W33: RP2354B, Package_DFN_QFN:QFN-80-1EP_10x10mm_P0.4mm_EP5.45x5.45mm, F.Cu at (18.0, 80.0)
- added U_W34: RP2354B, Package_DFN_QFN:QFN-80-1EP_10x10mm_P0.4mm_EP5.45x5.45mm, F.Cu at (33.0, 80.0)
- added U_W35: RP2354B, Package_DFN_QFN:QFN-80-1EP_10x10mm_P0.4mm_EP5.45x5.45mm, F.Cu at (48.0, 80.0)
- added U_W36: RP2354B, Package_DFN_QFN:QFN-80-1EP_10x10mm_P0.4mm_EP5.45x5.45mm, F.Cu at (63.0, 80.0)
- added U_W37: RP2354B, Package_DFN_QFN:QFN-80-1EP_10x10mm_P0.4mm_EP5.45x5.45mm, F.Cu at (78.0, 80.0)
- added U_W38: RP2354B, Package_DFN_QFN:QFN-80-1EP_10x10mm_P0.4mm_EP5.45x5.45mm, F.Cu at (93.0, 80.0)
- added U_W39: RP2354B, Package_DFN_QFN:QFN-80-1EP_10x10mm_P0.4mm_EP5.45x5.45mm, F.Cu at (108.0, 80.0)
- added U_W4: RP2354B, Package_DFN_QFN:QFN-80-1EP_10x10mm_P0.4mm_EP5.45x5.45mm, F.Cu at (78.0, 35.0)
- added U_W40: RP2354B, Package_DFN_QFN:QFN-80-1EP_10x10mm_P0.4mm_EP5.45x5.45mm, F.Cu at (123.0, 80.0)
- added U_W41: RP2354B, Package_DFN_QFN:QFN-80-1EP_10x10mm_P0.4mm_EP5.45x5.45mm, F.Cu at (138.0, 80.0)
- added U_W42: RP2354B, Package_DFN_QFN:QFN-80-1EP_10x10mm_P0.4mm_EP5.45x5.45mm, F.Cu at (153.0, 80.0)
- added U_W43: RP2354B, Package_DFN_QFN:QFN-80-1EP_10x10mm_P0.4mm_EP5.45x5.45mm, F.Cu at (168.0, 80.0)
- added U_W44: RP2354B, Package_DFN_QFN:QFN-80-1EP_10x10mm_P0.4mm_EP5.45x5.45mm, F.Cu at (18.0, 95.0)
- added U_W45: RP2354B, Package_DFN_QFN:QFN-80-1EP_10x10mm_P0.4mm_EP5.45x5.45mm, F.Cu at (33.0, 95.0)
- added U_W46: RP2354B, Package_DFN_QFN:QFN-80-1EP_10x10mm_P0.4mm_EP5.45x5.45mm, F.Cu at (48.0, 95.0)
- added U_W47: RP2354B, Package_DFN_QFN:QFN-80-1EP_10x10mm_P0.4mm_EP5.45x5.45mm, F.Cu at (63.0, 95.0)
- added U_W48: RP2354B, Package_DFN_QFN:QFN-80-1EP_10x10mm_P0.4mm_EP5.45x5.45mm, F.Cu at (78.0, 95.0)
- added U_W49: RP2354B, Package_DFN_QFN:QFN-80-1EP_10x10mm_P0.4mm_EP5.45x5.45mm, F.Cu at (93.0, 95.0)
- added U_W5: RP2354B, Package_DFN_QFN:QFN-80-1EP_10x10mm_P0.4mm_EP5.45x5.45mm, F.Cu at (93.0, 35.0)
- added U_W50: RP2354B, Package_DFN_QFN:QFN-80-1EP_10x10mm_P0.4mm_EP5.45x5.45mm, F.Cu at (108.0, 95.0)
- added U_W51: RP2354B, Package_DFN_QFN:QFN-80-1EP_10x10mm_P0.4mm_EP5.45x5.45mm, F.Cu at (123.0, 95.0)
- added U_W52: RP2354B, Package_DFN_QFN:QFN-80-1EP_10x10mm_P0.4mm_EP5.45x5.45mm, F.Cu at (138.0, 95.0)
- added U_W53: RP2354B, Package_DFN_QFN:QFN-80-1EP_10x10mm_P0.4mm_EP5.45x5.45mm, F.Cu at (153.0, 95.0)
- added U_W54: RP2354B, Package_DFN_QFN:QFN-80-1EP_10x10mm_P0.4mm_EP5.45x5.45mm, F.Cu at (168.0, 95.0)
- added U_W55: RP2354B, Package_DFN_QFN:QFN-80-1EP_10x10mm_P0.4mm_EP5.45x5.45mm, F.Cu at (18.0, 110.0)
- added U_W5500: W5500, Package_DFN_QFN:QFN-48-1EP_7x7mm_P0.5mm_EP5.15x5.15mm, F.Cu at (50.0, 185.0)
- added U_W56: RP2354B, Package_DFN_QFN:QFN-80-1EP_10x10mm_P0.4mm_EP5.45x5.45mm, F.Cu at (33.0, 110.0)
- added U_W57: RP2354B, Package_DFN_QFN:QFN-80-1EP_10x10mm_P0.4mm_EP5.45x5.45mm, F.Cu at (48.0, 110.0)
- added U_W58: RP2354B, Package_DFN_QFN:QFN-80-1EP_10x10mm_P0.4mm_EP5.45x5.45mm, F.Cu at (63.0, 110.0)
- added U_W59: RP2354B, Package_DFN_QFN:QFN-80-1EP_10x10mm_P0.4mm_EP5.45x5.45mm, F.Cu at (78.0, 110.0)
- added U_W6: RP2354B, Package_DFN_QFN:QFN-80-1EP_10x10mm_P0.4mm_EP5.45x5.45mm, F.Cu at (108.0, 35.0)
- added U_W60: RP2354B, Package_DFN_QFN:QFN-80-1EP_10x10mm_P0.4mm_EP5.45x5.45mm, F.Cu at (93.0, 110.0)
- added U_W61: RP2354B, Package_DFN_QFN:QFN-80-1EP_10x10mm_P0.4mm_EP5.45x5.45mm, F.Cu at (108.0, 110.0)
- added U_W62: RP2354B, Package_DFN_QFN:QFN-80-1EP_10x10mm_P0.4mm_EP5.45x5.45mm, F.Cu at (123.0, 110.0)
- added U_W63: RP2354B, Package_DFN_QFN:QFN-80-1EP_10x10mm_P0.4mm_EP5.45x5.45mm, F.Cu at (138.0, 110.0)
- added U_W64: RP2354B, Package_DFN_QFN:QFN-80-1EP_10x10mm_P0.4mm_EP5.45x5.45mm, F.Cu at (153.0, 110.0)
- added U_W65: RP2354B, Package_DFN_QFN:QFN-80-1EP_10x10mm_P0.4mm_EP5.45x5.45mm, F.Cu at (168.0, 110.0)
- added U_W66: RP2354B, Package_DFN_QFN:QFN-80-1EP_10x10mm_P0.4mm_EP5.45x5.45mm, F.Cu at (18.0, 125.0)
- added U_W67: RP2354B, Package_DFN_QFN:QFN-80-1EP_10x10mm_P0.4mm_EP5.45x5.45mm, F.Cu at (33.0, 125.0)
- added U_W68: RP2354B, Package_DFN_QFN:QFN-80-1EP_10x10mm_P0.4mm_EP5.45x5.45mm, F.Cu at (48.0, 125.0)
- added U_W69: RP2354B, Package_DFN_QFN:QFN-80-1EP_10x10mm_P0.4mm_EP5.45x5.45mm, F.Cu at (63.0, 125.0)
- added U_W7: RP2354B, Package_DFN_QFN:QFN-80-1EP_10x10mm_P0.4mm_EP5.45x5.45mm, F.Cu at (123.0, 35.0)
- added U_W70: RP2354B, Package_DFN_QFN:QFN-80-1EP_10x10mm_P0.4mm_EP5.45x5.45mm, F.Cu at (78.0, 125.0)
- added U_W71: RP2354B, Package_DFN_QFN:QFN-80-1EP_10x10mm_P0.4mm_EP5.45x5.45mm, F.Cu at (93.0, 125.0)
- added U_W72: RP2354B, Package_DFN_QFN:QFN-80-1EP_10x10mm_P0.4mm_EP5.45x5.45mm, F.Cu at (108.0, 125.0)
- added U_W73: RP2354B, Package_DFN_QFN:QFN-80-1EP_10x10mm_P0.4mm_EP5.45x5.45mm, F.Cu at (123.0, 125.0)
- added U_W74: RP2354B, Package_DFN_QFN:QFN-80-1EP_10x10mm_P0.4mm_EP5.45x5.45mm, F.Cu at (138.0, 125.0)
- added U_W75: RP2354B, Package_DFN_QFN:QFN-80-1EP_10x10mm_P0.4mm_EP5.45x5.45mm, F.Cu at (153.0, 125.0)
- added U_W76: RP2354B, Package_DFN_QFN:QFN-80-1EP_10x10mm_P0.4mm_EP5.45x5.45mm, F.Cu at (168.0, 125.0)
- added U_W77: RP2354B, Package_DFN_QFN:QFN-80-1EP_10x10mm_P0.4mm_EP5.45x5.45mm, F.Cu at (18.0, 140.0)
- added U_W78: RP2354B, Package_DFN_QFN:QFN-80-1EP_10x10mm_P0.4mm_EP5.45x5.45mm, F.Cu at (33.0, 140.0)
- added U_W79: RP2354B, Package_DFN_QFN:QFN-80-1EP_10x10mm_P0.4mm_EP5.45x5.45mm, F.Cu at (48.0, 140.0)
- added U_W8: RP2354B, Package_DFN_QFN:QFN-80-1EP_10x10mm_P0.4mm_EP5.45x5.45mm, F.Cu at (138.0, 35.0)
- added U_W80: RP2354B, Package_DFN_QFN:QFN-80-1EP_10x10mm_P0.4mm_EP5.45x5.45mm, F.Cu at (63.0, 140.0)
- added U_W81: RP2354B, Package_DFN_QFN:QFN-80-1EP_10x10mm_P0.4mm_EP5.45x5.45mm, F.Cu at (78.0, 140.0)
- added U_W82: RP2354B, Package_DFN_QFN:QFN-80-1EP_10x10mm_P0.4mm_EP5.45x5.45mm, F.Cu at (93.0, 140.0)
- added U_W83: RP2354B, Package_DFN_QFN:QFN-80-1EP_10x10mm_P0.4mm_EP5.45x5.45mm, F.Cu at (108.0, 140.0)
- added U_W84: RP2354B, Package_DFN_QFN:QFN-80-1EP_10x10mm_P0.4mm_EP5.45x5.45mm, F.Cu at (123.0, 140.0)
- added U_W85: RP2354B, Package_DFN_QFN:QFN-80-1EP_10x10mm_P0.4mm_EP5.45x5.45mm, F.Cu at (138.0, 140.0)
- added U_W86: RP2354B, Package_DFN_QFN:QFN-80-1EP_10x10mm_P0.4mm_EP5.45x5.45mm, F.Cu at (153.0, 140.0)
- added U_W87: RP2354B, Package_DFN_QFN:QFN-80-1EP_10x10mm_P0.4mm_EP5.45x5.45mm, F.Cu at (168.0, 140.0)
- added U_W88: RP2354B, Package_DFN_QFN:QFN-80-1EP_10x10mm_P0.4mm_EP5.45x5.45mm, F.Cu at (18.0, 155.0)
- added U_W89: RP2354B, Package_DFN_QFN:QFN-80-1EP_10x10mm_P0.4mm_EP5.45x5.45mm, F.Cu at (33.0, 155.0)
- added U_W9: RP2354B, Package_DFN_QFN:QFN-80-1EP_10x10mm_P0.4mm_EP5.45x5.45mm, F.Cu at (153.0, 35.0)
- added U_W90: RP2354B, Package_DFN_QFN:QFN-80-1EP_10x10mm_P0.4mm_EP5.45x5.45mm, F.Cu at (48.0, 155.0)
- added U_W91: RP2354B, Package_DFN_QFN:QFN-80-1EP_10x10mm_P0.4mm_EP5.45x5.45mm, F.Cu at (63.0, 155.0)
- added U_W92: RP2354B, Package_DFN_QFN:QFN-80-1EP_10x10mm_P0.4mm_EP5.45x5.45mm, F.Cu at (78.0, 155.0)
- added U_W93: RP2354B, Package_DFN_QFN:QFN-80-1EP_10x10mm_P0.4mm_EP5.45x5.45mm, F.Cu at (93.0, 155.0)
- added U_W94: RP2354B, Package_DFN_QFN:QFN-80-1EP_10x10mm_P0.4mm_EP5.45x5.45mm, F.Cu at (108.0, 155.0)
- added U_W95: RP2354B, Package_DFN_QFN:QFN-80-1EP_10x10mm_P0.4mm_EP5.45x5.45mm, F.Cu at (123.0, 155.0)
- added U_W96: RP2354B, Package_DFN_QFN:QFN-80-1EP_10x10mm_P0.4mm_EP5.45x5.45mm, F.Cu at (138.0, 155.0)
- added U_W97: RP2354B, Package_DFN_QFN:QFN-80-1EP_10x10mm_P0.4mm_EP5.45x5.45mm, F.Cu at (153.0, 155.0)
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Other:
- board text added: "74HC595 x14 CS Cascade"
- board text added: "BOOTSTRAP (14x PCF8574)"
- board text added: "CLK TREE (14x 74HC244)"
- board text added: "FPGA iCE40HX4K"
- board text added: "MicroSD x5 RAID-0"
- board text added: "POWER (12V/PoE) 4x TPS54560"
- board text added: "PSRAM (110x SOP-8 on B.Cu)"
- board text added: "RJ45 PoE"
- board text added: "RP2354 110-Node Network Compute Fabric v1.0"
- board text added: "USB-C"
- board text added: "W0"
- board text added: "W1"
- board text added: "W10"
- board text added: "W100"
- board text added: "W101"
- board text added: "W102"
- board text added: "W103"
- board text added: "W104"
- board text added: "W105"
- board text added: "W106"
- board text added: "W107"
- board text added: "W108"
- board text added: "W109"
- board text added: "W11"
- board text added: "W12"
- board text added: "W13"
- board text added: "W14"
- board text added: "W15"
- board text added: "W16"
- board text added: "W17"
- board text added: "W18"
- board text added: "W19"
- board text added: "W2"
- board text added: "W20"
- board text added: "W21"
- board text added: "W22"
- board text added: "W23"
- board text added: "W24"
- board text added: "W25"
- board text added: "W26"
- board text added: "W27"
- board text added: "W28"
- board text added: "W29"
- board text added: "W3"
- board text added: "W30"
- board text added: "W31"
- board text added: "W32"
- board text added: "W33"
- board text added: "W34"
- board text added: "W35"
- board text added: "W36"
- board text added: "W37"
- board text added: "W38"
- board text added: "W39"
- board text added: "W4"
- board text added: "W40"
- board text added: "W41"
- board text added: "W42"
- board text added: "W43"
- board text added: "W44"
- board text added: "W45"
- board text added: "W46"
- board text added: "W47"
- board text added: "W48"
- board text added: "W49"
- board text added: "W5"
- board text added: "W50"
- board text added: "W51"
- board text added: "W52"
- board text added: "W53"
- board text added: "W54"
- board text added: "W55"
- board text added: "W5500 Ethernet"
- board text added: "W56"
- board text added: "W57"
- board text added: "W58"
- board text added: "W59"
- board text added: "W6"
- board text added: "W60"
- board text added: "W61"
- board text added: "W62"
- board text added: "W63"
- board text added: "W64"
- board text added: "W65"
- board text added: "W66"
- board text added: "W67"
- board text added: "W68"
- board text added: "W69"
- board text added: "W7"
- board text added: "W70"
- board text added: "W71"
- board text added: "W72"
- board text added: "W73"
- board text added: "W74"
- board text added: "W75"
- board text added: "W76"
- board text added: "W77"
- board text added: "W78"
- board text added: "W79"
- board text added: "W8"
- board text added: "W80"
- board text added: "W81"
- board text added: "W82"
- board text added: "W83"
- board text added: "W84"
- board text added: "W85"
- board text added: "W86"
- board text added: "W87"
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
